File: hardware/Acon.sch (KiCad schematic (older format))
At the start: 12 parts, among them U1 AD620, U2 REF1004-2.5

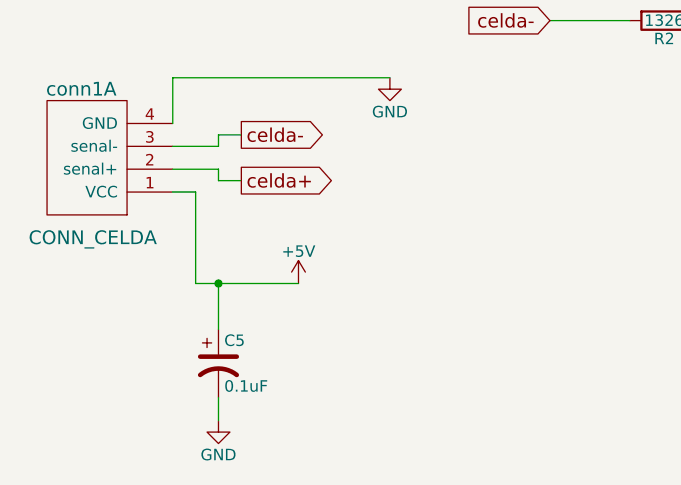
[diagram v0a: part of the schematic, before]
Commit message: Se finalizo esquematico del cricuito.
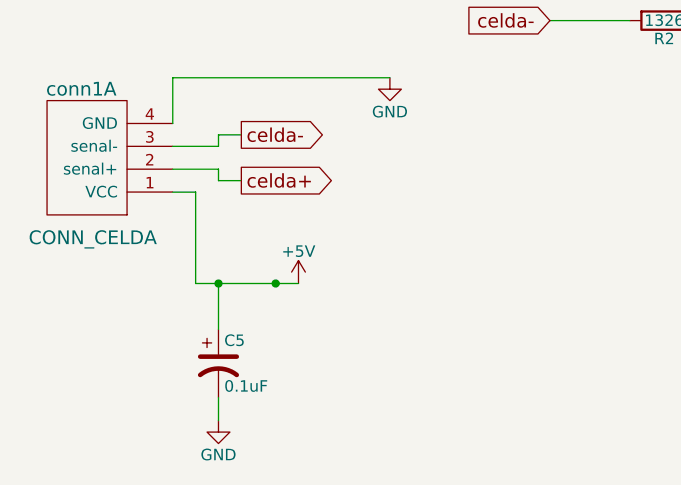
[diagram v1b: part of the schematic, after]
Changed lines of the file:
@@
 encoding utf-8
 Sheet 3 5
-Title ""
-Date ""
+Title "Diagrama de acondicionamiento de señal."
+Date "2016-07-04"
 Rev ""
-Comp ""
+Comp "Felipe Rey"
 Comment1 ""
 Comment2 ""
@@
 $EndComp
 $Comp
-L +5V #PWR?
+L +5V #PWR06
 U 1 1 57856E05
 P 7400 2100
-F 0 "#PWR?" H 7400 1950 50  0001 C CNN
+F 0 "#PWR06" H 7400 1950 50  0001 C CNN
 F 1 "+5V" H 7400 2240 50  0000 C CNN
 F 2 "" H 7400 2100 60  0000 C CNN
@@
 $EndComp
 $Comp
-L GND #PWR?
+L GND #PWR07
 U 1 1 57856E1C
 P 7150 4250
-F 0 "#PWR?" H 7150 4000 50  0001 C CNN
+F 0 "#PWR07" H 7150 4000 50  0001 C CNN
 F 1 "GND" H 7150 4100 50  0000 C CNN
 F 2 "" H 7150 4250 60  0000 C CNN
@@
 $EndComp
 $Comp
-L GND #PWR?
+L GND #PWR08
 U 1 1 578576D0
 P 6600 4250
-F 0 "#PWR?" H 6600 4000 50  0001 C CNN
+F 0 "#PWR08" H 6600 4000 50  0001 C CNN
 F 1 "GND" H 6600 4100 50  0000 C CNN
 F 2 "" H 6600 4250 60  0000 C CNN
@@
 $EndComp
 $Comp
-L GND #PWR?
+L GND #PWR09
 U 1 1 57857780
 P 6300 2650
-F 0 "#PWR?" H 6300 2400 50  0001 C CNN
+F 0 "#PWR09" H 6300 2400 50  0001 C CNN
 F 1 "GND" H 6300 2500 50  0000 C CNN
 F 2 "" H 6300 2650 60  0000 C CNN
@@
 $EndComp
 $Comp
-L GND #PWR?
+L GND #PWR010
 U 1 1 57857C0A
 P 7800 2800
-F 0 "#PWR?" H 7800 2550 50  0001 C CNN
+F 0 "#PWR010" H 7800 2550 50  0001 C CNN
 F 1 "GND" H 7800 2650 50  0000 C CNN
 F 2 "" H 7800 2800 60  0000 C CNN
@@
 $EndComp
 $Comp
-L GND #PWR?
+L GND #PWR011
 U 1 1 57858D35
 P 3500 2800
-F 0 "#PWR?" H 3500 2550 50  0001 C CNN
+F 0 "#PWR011" H 3500 2550 50  0001 C CNN
 F 1 "GND" H 3500 2650 50  0000 C CNN
 F 2 "" H 3500 2800 60  0000 C CNN
@@
 ref_2_5
 $Comp
-L +5V #PWR?
+L +5V #PWR012
 U 1 1 5785922C
 P 5550 1850
-F 0 "#PWR?" H 5550 1700 50  0001 C CNN
+F 0 "#PWR012" H 5550 1700 50  0001 C CNN
 F 1 "+5V" H 5550 1990 50  0000 C CNN
 F 2 "" H 5550 1850 60  0000 C CNN
@@
 $EndComp
 $Comp
-L GND #PWR?
+L GND #PWR013
 U 1 1 5785A32A
 P 4150 5400
-F 0 "#PWR?" H 4150 5150 50  0001 C CNN
+F 0 "#PWR013" H 4150 5150 50  0001 C CNN
 F 1 "GND" H 4150 5250 50  0000 C CNN
 F 2 "" H 4150 5400 60  0000 C CNN
@@
 $EndComp
 $Comp
-L GND #PWR?
+L GND #PWR014
 U 1 1 5785A356
 P 4900 3900
-F 0 "#PWR?" H 4900 3650 50  0001 C CNN
+F 0 "#PWR014" H 4900 3650 50  0001 C CNN
 F 1 "GND" H 4900 3750 50  0000 C CNN
 F 2 "" H 4900 3900 60  0000 C CNN
@@
 	4150 5300 4150 5400
 $Comp
-L +5V #PWR?
+L +5V #PWR015
 U 1 1 5785AD35
 P 4500 4800
-F 0 "#PWR?" H 4500 4650 50  0001 C CNN
+F 0 "#PWR015" H 4500 4650 50  0001 C CNN
 F 1 "+5V" H 4500 4940 50  0000 C CNN
 F 2 "" H 4500 4800 60  0000 C CNN
@@
 Wire Wire Line
 	7800 3450 8200 3450
+Connection ~ 4400 4800
 $EndSCHEMATC

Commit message: Se cargaron los footprint de los componentes.
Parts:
- C1, C2, C3: footprint (none) -> ej2cese:C_0603_HandSoldering
- C4, C5: footprint (none) -> Capacitors_SMD:C_0805
- R1, R2, R3, R4: footprint (none) -> ej2cese:R_1206_HandSoldering
- U1, U2: footprint (none) -> SMD_Packages:SOIC-8-N
- conn1: footprint (none) -> Connect:bornier4
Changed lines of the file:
@@
 LIBS:valves
 LIBS:ej2cese
+LIBS:ADS1113IDGSR
 LIBS:poncho_celda-cache
 EELAYER 25 0
@@
 F 0 "U1" H 7800 3700 70  0000 C CNN
 F 1 "AD620" H 7900 3200 70  0000 C CNN
-F 2 "" H 7500 3450 60  0000 C CNN
+F 2 "SMD_Packages:SOIC-8-N" H 7500 3450 60  0001 C CNN
 F 3 "" H 7500 3450 60  0000 C CNN
 	1    7500 3450
@@
 F 0 "C1" H 6625 3050 50  0000 L CNN
 F 1 "0.001uF" H 6625 2850 50  0000 L CNN
-F 2 "" H 6638 2800 30  0000 C CNN
+F 2 "ej2cese:C_0603_HandSoldering" H 6638 2800 30  0001 C CNN
 F 3 "" H 6600 2950 60  0000 C CNN
 	1    6600 2950
@@
 F 0 "C2" H 6625 3500 50  0000 L CNN
 F 1 "0.01uF" H 6625 3300 50  0000 L CNN
-F 2 "" H 6638 3250 30  0000 C CNN
+F 2 "ej2cese:C_0603_HandSoldering" H 6638 3250 30  0001 C CNN
 F 3 "" H 6600 3400 60  0000 C CNN
 	1    6600 3400
@@
 F 0 "C3" H 6625 4050 50  0000 L CNN
 F 1 "0.001uF" H 6625 3850 50  0000 L CNN
-F 2 "" H 6638 3800 30  0000 C CNN
+F 2 "ej2cese:C_0603_HandSoldering" H 6638 3800 30  0001 C CNN
 F 3 "" H 6600 3950 60  0000 C CNN
 	1    6600 3950
@@
 F 0 "R1" V 6180 3200 50  0000 C CNN
 F 1 "1326" V 6100 3200 50  0000 C CNN
-F 2 "" V 6030 3200 30  0000 C CNN
+F 2 "ej2cese:R_1206_HandSoldering" V 6030 3200 30  0001 C CNN
 F 3 "" H 6100 3200 30  0000 C CNN
 	1    6100 3200
@@
 F 0 "R2" V 6180 3650 50  0000 C CNN
 F 1 "1326" V 6100 3650 50  0000 C CNN
-F 2 "" V 6030 3650 30  0000 C CNN
+F 2 "ej2cese:R_1206_HandSoldering" V 6030 3650 30  0001 C CNN
 F 3 "" H 6100 3650 30  0000 C CNN
 	1    6100 3650
@@
 F 0 "C4" H 7825 2600 50  0000 L CNN
 F 1 "0.1uF" H 7825 2400 50  0000 L CNN
-F 2 "" H 7800 2500 60  0000 C CNN
+F 2 "Capacitors_SMD:C_0805" H 7800 2500 60  0001 C CNN
 F 3 "" H 7800 2500 60  0000 C CNN
 	1    7800 2500
@@
 F 0 "R3" V 7680 4150 50  0000 C CNN
 F 1 "500" V 7600 4150 50  0000 C CNN
-F 2 "" V 7530 4150 30  0000 C CNN
+F 2 "ej2cese:R_1206_HandSoldering" V 7530 4150 30  0001 C CNN
 F 3 "" H 7600 4150 30  0000 C CNN
 	1    7600 4150
@@
 F 0 "U2" H 4300 1900 60  0000 C CNN
 F 1 "REF1004-2.5" H 4250 2750 60  0000 C CNN
-F 2 "" H 4300 2100 60  0000 C CNN
+F 2 "SMD_Packages:SOIC-8-N" H 4300 2100 60  0001 C CNN
 F 3 "" H 4300 2100 60  0000 C CNN
 	1    4300 2350
@@
 F 0 "R4" V 5330 2150 50  0000 C CNN
 F 1 "50k" V 5250 2150 50  0000 C CNN
-F 2 "" V 5180 2150 30  0000 C CNN
+F 2 "ej2cese:R_1206_HandSoldering" V 5180 2150 30  0001 C CNN
 F 3 "" H 5250 2150 30  0000 C CNN
 	1    5250 2150
@@
 F 0 "conn1" H 3650 3950 60  0000 C CNN
 F 1 "CONN_CELDA" H 3600 4600 60  0000 C CNN
-F 2 "" H 3600 4050 60  0000 C CNN
+F 2 "Connect:bornier4" H 3600 4050 60  0001 C CNN
 F 3 "" H 3600 4050 60  0000 C CNN
 	1    3600 4300
@@
 F 0 "C5" H 4175 5250 50  0000 L CNN
 F 1 "0.1uF" H 4175 5050 50  0000 L CNN
-F 2 "" H 4150 5150 60  0000 C CNN
+F 2 "Capacitors_SMD:C_0805" H 4150 5150 60  0001 C CNN
 F 3 "" H 4150 5150 60  0000 C CNN
 	1    4150 5150

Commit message: Se realizan correcciones al esquematico.
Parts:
- added C6: 100nF, celda:C_0805_HandSoldering, symbol CP1
- added R5, R6: 1k, celda:R_1206_HandSoldering, symbol R
- added U3: ADS1113/15, celda:TSSOP-10_3x3mm_Pitch0.5mm, symbol ADS1113/15
- C1, C3: value 0.001uF -> 1nF; footprint ej2cese:C_0603_HandSoldering -> celda:C_0603_HandSoldering
- C2: value 0.01uF -> 10nF; footprint ej2cese:C_0603_HandSoldering -> celda:C_0603_HandSoldering
- C4, C5: value 0.1uF -> 100nF; footprint Capacitors_SMD:C_0805 -> celda:C_0805_HandSoldering
- R1, R2: value 1326 -> 1k; footprint ej2cese:R_1206_HandSoldering -> celda:R_1206_HandSoldering
- R3: value 500 -> 499; footprint ej2cese:R_1206_HandSoldering -> celda:R_1206_HandSoldering
- R4: value 50k -> 51k; footprint ej2cese:R_1206_HandSoldering -> celda:R_1206_HandSoldering
- U1, U2: footprint SMD_Packages:SOIC-8-N -> celda:SOIC-8
- conn1: footprint Connect:bornier4 -> celda:bornier4
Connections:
- net +5V: now also C6.1, U3.8 (VDD)
- net GND: now also C6.2, U3.1 (ADDR), U3.3 (GND)
- net celda+: no longer names the net of R1.2, conn1.2 (senal+)
- net celda-: no longer names the net of R2.2, conn1.3 (senal-)
- net celda_acond: no longer names the net of U1.6 (OUT)
- net celda_acond: now also U3.4 (AIN0)
- net ref_2_5: no longer names the net of U1.5 (Ref), U2.6 (Catodo_1)
- new net +3.3V: R5.1, R6.1
- new net alert: U3.2 (ALERT)
- new net scl: R5.2, U3.10 (SCL)
- new net sda: R6.2, U3.9 (SDA)
- no-connect marks 0 -> 3
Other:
- moved on the sheet: C1, C2, C3, C4, C5, R1, R2, R3, R4, U1, U2A, conn1A

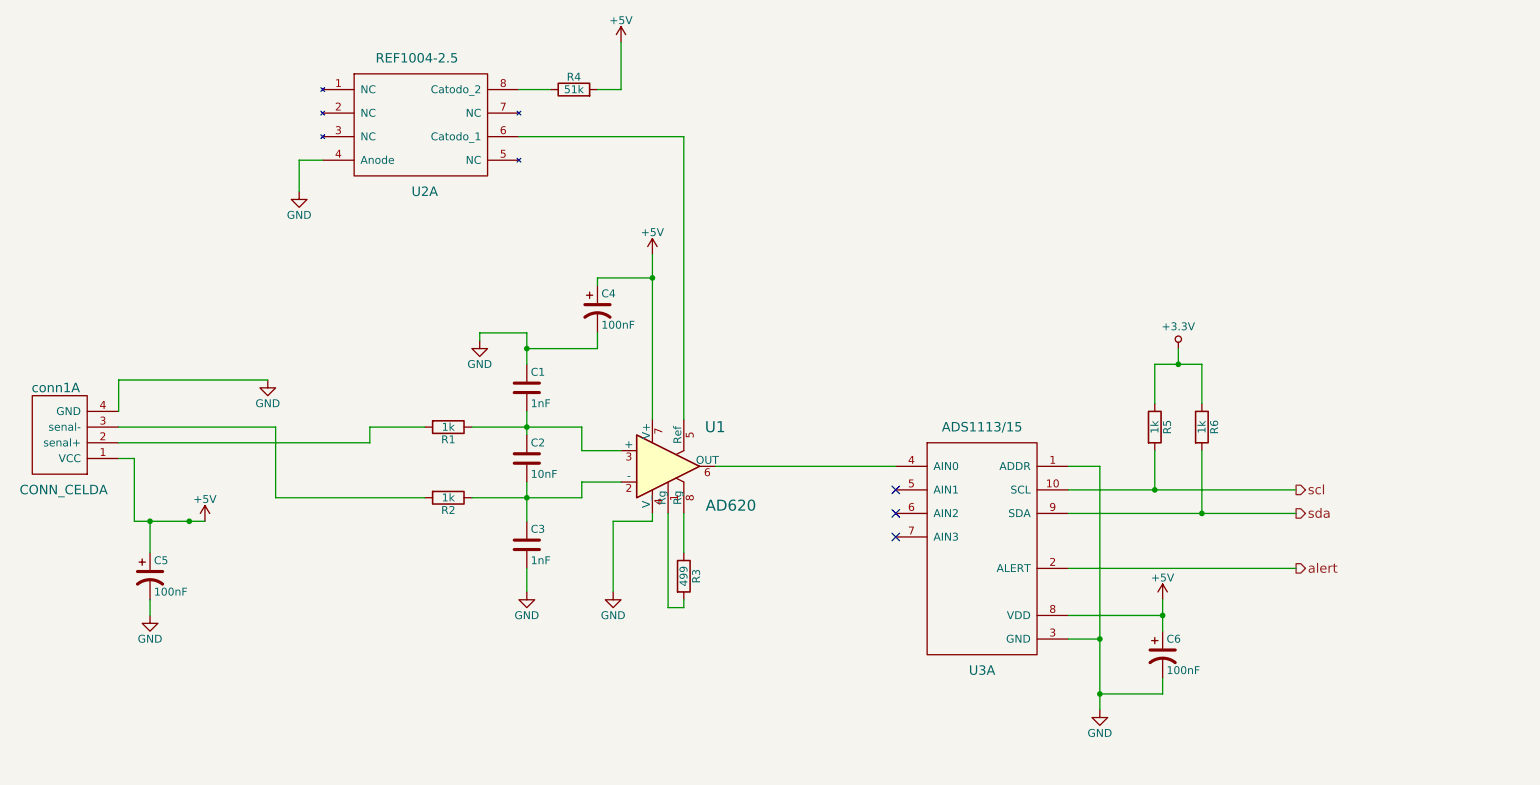
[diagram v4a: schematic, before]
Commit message: Se agregan componentes 3d.
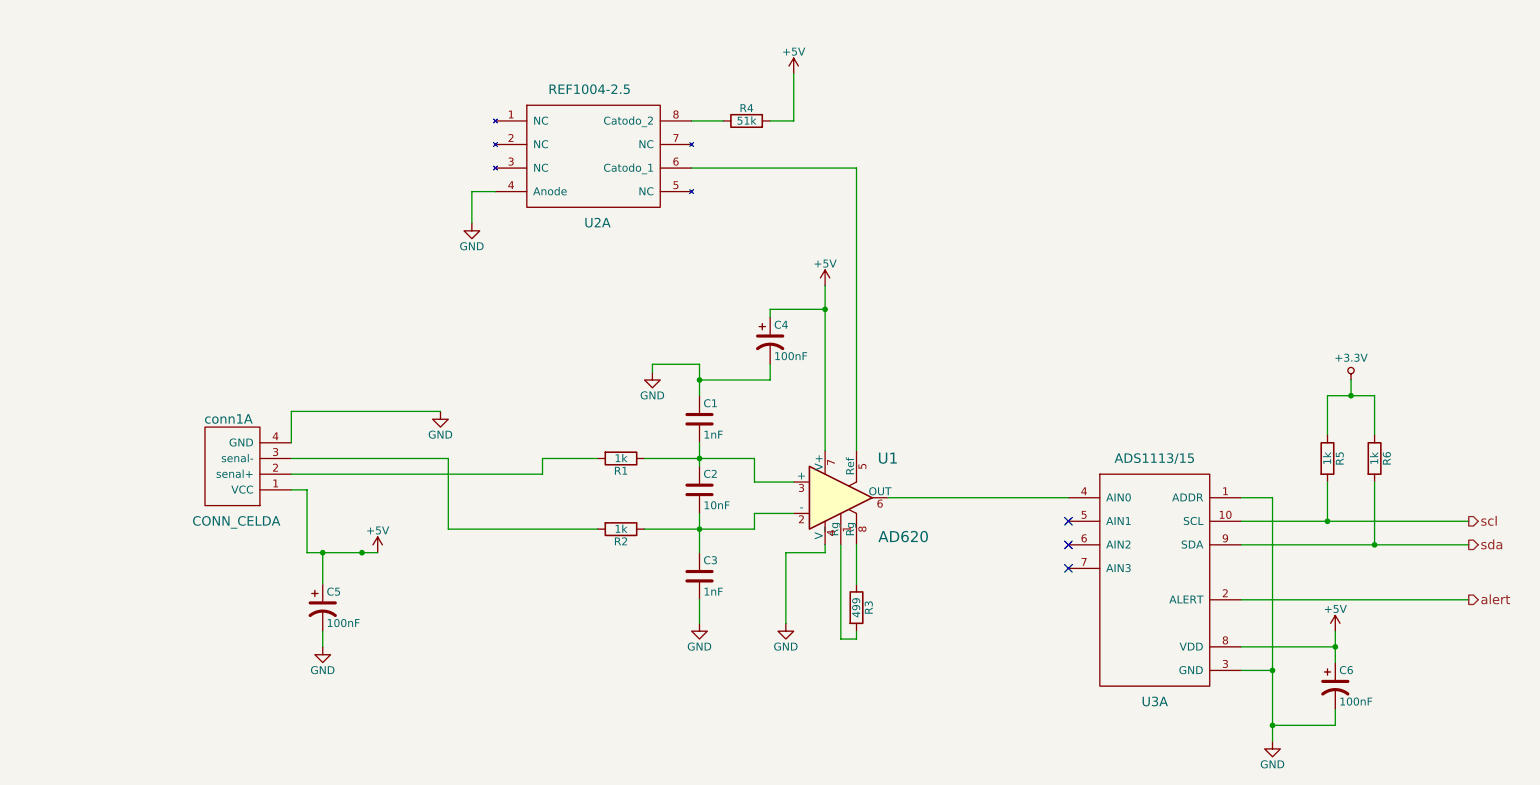
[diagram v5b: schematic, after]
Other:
- moved on the sheet: C1, C2, C3, C4, C5, C6, R1, R2, R3, R4, R5, R6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

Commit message: Correcciones en clases.
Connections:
- wire segments 61 -> 67
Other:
- moved on the sheet: C1
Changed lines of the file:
@@
 EESchema Schematic File Version 2
-LIBS:power
-LIBS:device
-LIBS:transistors
-LIBS:conn
-LIBS:linear
-LIBS:regul
-LIBS:74xx
-LIBS:cmos4000
-LIBS:adc-dac
-LIBS:memory
-LIBS:xilinx
-LIBS:microcontrollers
-LIBS:dsp
-LIBS:microchip
-LIBS:analog_switches
-LIBS:motorola
-LIBS:texas
-LIBS:intel
-LIBS:audio
-LIBS:interface
-LIBS:digital-audio
-LIBS:philips
-LIBS:display
-LIBS:cypress
-LIBS:siliconi
-LIBS:opto
-LIBS:atmel
-LIBS:contrib
-LIBS:valves
 LIBS:ej2cese
-LIBS:ADS1113IDGSR
 LIBS:poncho_celda-cache
 EELAYER 25 0
@@
 Rev ""
 Comp "Felipe Rey Hernandez"
-Comment1 "Diagrama esquematico de modulos para poncho celda para el curso de Diseño de PCB del CESE."
+Comment1 "Esquematico de modulos para poncho celda para el curso de Diseño de PCB del CESE."
 Comment2 "Licencia GPL V3"
 Comment3 ""
@@
 $EndComp
 $Comp
-L C C1
-U 1 1 57856F17
-P 5150 3350
-F 0 "C1" H 5175 3450 50  0000 L CNN
-F 1 "1nF" H 5175 3250 50  0000 L CNN
-F 2 "celda:C_0603_HandSoldering" H 5188 3200 30  0001 C CNN
-F 3 "" H 5150 3350 60  0000 C CNN
-	1    5150 3350
-	1    0    0    -1
-$EndComp
-$Comp
 L C C2
 U 1 1 57856F86
@@
 L GND #PWR08
 U 1 1 57857780
-P 4850 3050
-F 0 "#PWR08" H 4850 2800 50  0001 C CNN
-F 1 "GND" H 4850 2900 50  0000 C CNN
-F 2 "" H 4850 3050 60  0000 C CNN
-F 3 "" H 4850 3050 60  0000 C CNN
-	1    4850 3050
+P 4850 3000
+F 0 "#PWR08" H 4850 2750 50  0001 C CNN
+F 1 "GND" H 4850 2850 50  0000 C CNN
+F 2 "" H 4850 3000 60  0000 C CNN
+F 3 "" H 4850 3000 60  0000 C CNN
+	1    4850 3000
 	1    0    0    -1
 $EndComp
@@
 $EndComp
 Wire Wire Line
-	5500 3750 5750 3750
-Wire Wire Line
-	5500 3600 5500 3750
-Wire Wire Line
-	4800 3600 5500 3600
-Wire Wire Line
-	5150 3500 5150 3650
-Connection ~ 5150 3600
-Wire Wire Line
-	5500 3950 5750 3950
-Wire Wire Line
-	5500 4050 5500 3950
-Wire Wire Line
-	4800 4050 5500 4050
-Wire Wire Line
-	5150 3950 5150 4200
-Connection ~ 5150 4050
-Wire Wire Line
-	5150 3200 5150 3000
-Wire Wire Line
-	5150 3000 4850 3000
-Wire Wire Line
-	4850 3000 4850 3050
-Wire Wire Line
-	5150 4500 5150 4650
+	5500 3550 5500 3750
+Wire Wire Line
+	5500 4100 5500 3950
+Wire Wire Line
+	5150 2950 4850 2950
+Wire Wire Line
+	4850 2950 4850 3000
 Wire Wire Line
 	5950 2500 5950 3550
@@
 	6150 1750 6150 3550
 Wire Wire Line
-	4150 3600 4500 3600
-Wire Wire Line
-	3550 4050 4500 4050
-Wire Wire Line
 	5950 4150 5950 4200
 Wire Wire Line
@@
 	5700 4200 5700 4650
 Wire Wire Line
-	6150 4400 6150 4150
-Wire Wire Line
-	6050 4150 6050 4750
-Wire Wire Line
-	6050 4750 6150 4750
-Wire Wire Line
-	6150 4750 6150 4700
-Wire Wire Line
 	3850 1900 3700 1900
 Wire Wire Line
@@
 Wire Wire Line
 	5750 1150 5750 1450
-Wire Wire Line
-	5750 1450 5600 1450
-Wire Wire Line
-	5300 1450 5100 1450
 Wire Wire Line
 	5100 1750 6150 1750
@@
 	8600 4000 10050 4000
 Wire Wire Line
-	9150 4000 9150 3750
-Wire Wire Line
-	9450 3750 9450 4150
-Wire Wire Line
 	8600 4150 10050 4150
 $Comp
@@
 $EndComp
 Wire Wire Line
-	9150 3450 9150 3200
-Wire Wire Line
 	9150 3200 9450 3200
 Wire Wire Line
 	9300 3200 9300 3100
-Wire Wire Line
-	9450 3200 9450 3450
 Connection ~ 9300 3200
 $Comp
@@
 Connection ~ 5950 2650
 Wire Wire Line
+	5750 1450 5700 1450
+Wire Wire Line
+	5200 1450 5100 1450
+Wire Wire Line
+	4150 3600 4400 3600
+$Comp
+L C C1
+U 1 1 57856F17
+P 5150 3300
+F 0 "C1" H 5175 3400 50  0000 L CNN
+F 1 "1nF" H 5175 3200 50  0000 L CNN
+F 2 "celda:C_0603_HandSoldering" H 5188 3150 30  0001 C CNN
+F 3 "" H 5150 3300 60  0000 C CNN
+	1    5150 3300
+	1    0    0    -1
+$EndComp
+Wire Wire Line
+	5150 2950 5150 3100
+Wire Wire Line
 	5600 3000 5600 3100
 Wire Wire Line
-	5600 3100 5150 3100
-Connection ~ 5150 3100
+	5600 3100 5300 3100
+Wire Wire Line
+	5300 3100 5300 3000
+Wire Wire Line
+	5300 3000 5150 3000
+Connection ~ 5150 3000
+Wire Wire Line
+	5150 3500 5150 3600
+Wire Wire Line
+	4900 3600 5000 3600
+Wire Wire Line
+	5000 3600 5000 3550
+Wire Wire Line
+	5000 3550 5500 3550
+Connection ~ 5150 3550
+Wire Wire Line
+	5150 4650 5150 4550
+Wire Wire Line
+	3550 4050 4400 4050
+Wire Wire Line
+	5150 4150 5150 4000
+Wire Wire Line
+	4900 4050 5050 4050
+Wire Wire Line
+	5050 4050 5050 4100
+Wire Wire Line
+	5050 4100 5500 4100
+Connection ~ 5150 4100
+Wire Wire Line
+	5500 3950 5750 3950
+Wire Wire Line
+	5500 3750 5750 3750
+Wire Wire Line
+	9450 3850 9450 4150
+Wire Wire Line
+	9150 3850 9150 4000
+Wire Wire Line
+	9150 3200 9150 3350
+Wire Wire Line
+	9450 3200 9450 3350
+Wire Wire Line
+	6050 4150 6050 5050
+Wire Wire Line
+	6050 5050 6150 5050
+Wire Wire Line
+	6150 5050 6150 4800
+Wire Wire Line
+	6150 4300 6150 4150
 $EndSCHEMATC
